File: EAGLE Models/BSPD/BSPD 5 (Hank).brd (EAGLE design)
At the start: 15.2 x 102.9 mm, 23 parts, among them IC1 LT1236S-5

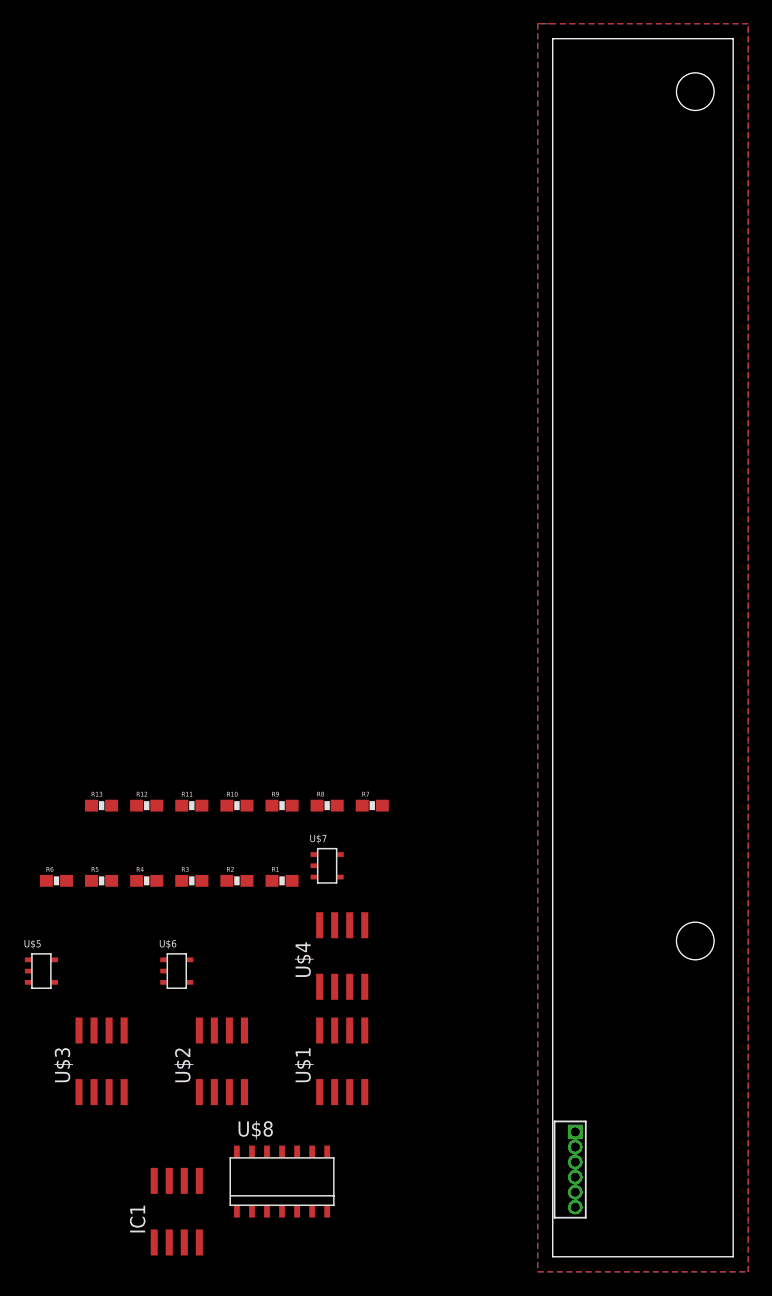
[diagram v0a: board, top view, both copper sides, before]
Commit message: BSPD board layout
Version 1, laying out v2 that should be theorectically more organized
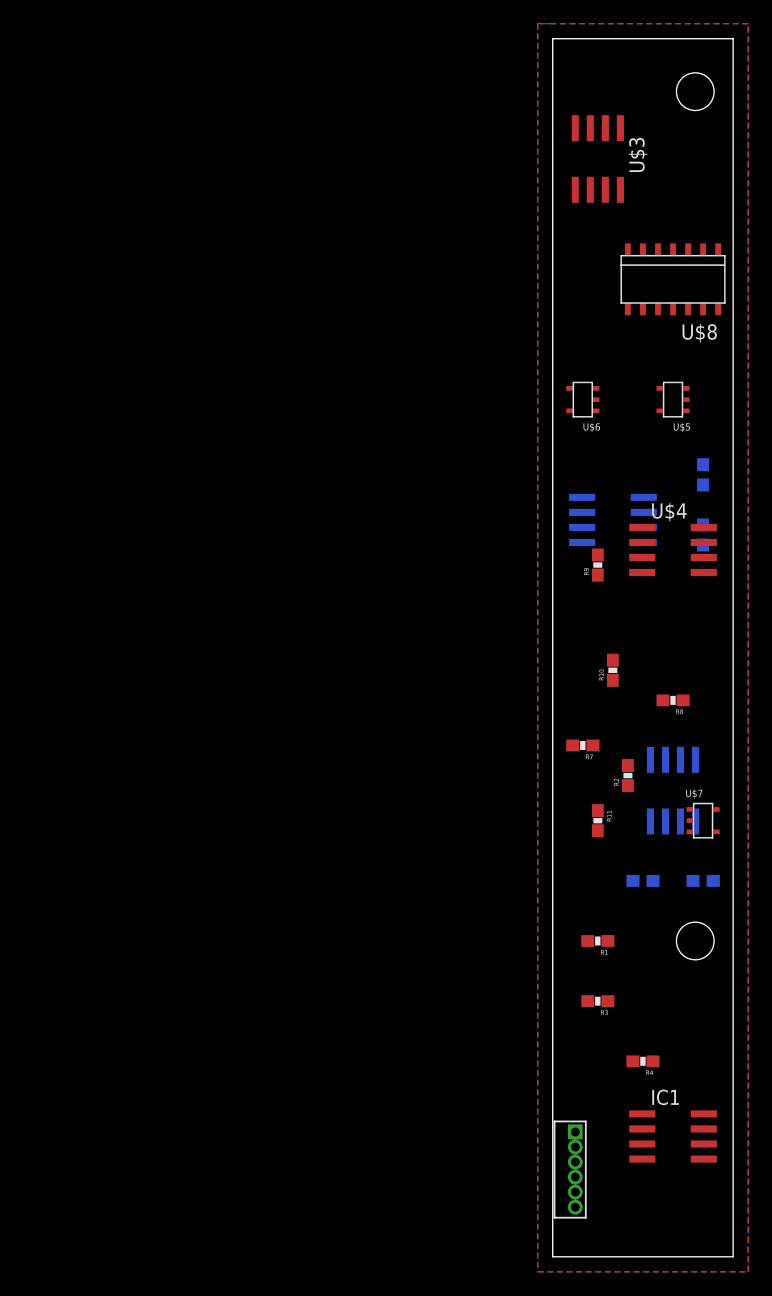
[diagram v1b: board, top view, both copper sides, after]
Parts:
- moved U$3 87.0 mm to (3.81, 92.7), turned to 180 degrees
- moved U$8 83.0 mm to (10.2, 82.5), turned to 180 degrees
- moved U$5 71.9 mm to (10.2, 72.4), turned to 180 degrees
- moved R6 64.5 mm to (12.7, 66.0), flipped to the bottom, turned to 270 degrees
- moved U$6 59.2 mm to (2.54, 72.4), turned to 180 degrees
- moved R5 58.6 mm to (12.7, 61.0), flipped to the bottom, turned to 270 degrees
- moved R13 51.2 mm to (12.7, 31.8), flipped to the bottom
- moved U$1 51.1 mm to (5.08, 62.2), flipped to the bottom, turned to 90 degrees
- moved R4 44.6 mm to (7.62, 16.5), turned to 180 degrees
- moved U$2 44.4 mm to (10.2, 39.4), flipped to the bottom, turned to 180 degrees
- moved U$4 44.2 mm to (10.2, 59.7), turned to 270 degrees
- moved IC1 42.4 mm to (10.2, 10.2), turned to 270 degrees
- moved R12 42.4 mm to (7.62, 31.8), flipped to the bottom, turned to 180 degrees
- moved R3 35.8 mm to (3.81, 21.6), turned to 180 degrees
- moved R11 34.3 mm to (3.81, 36.8), turned to 270 degrees
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
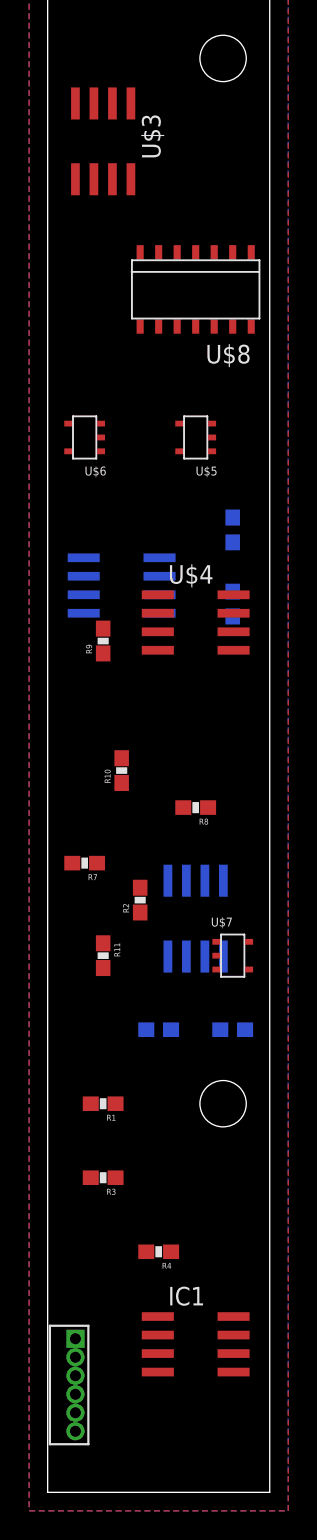
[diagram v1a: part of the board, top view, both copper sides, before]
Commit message: General layout of BSPD
Version 2, needs optimization
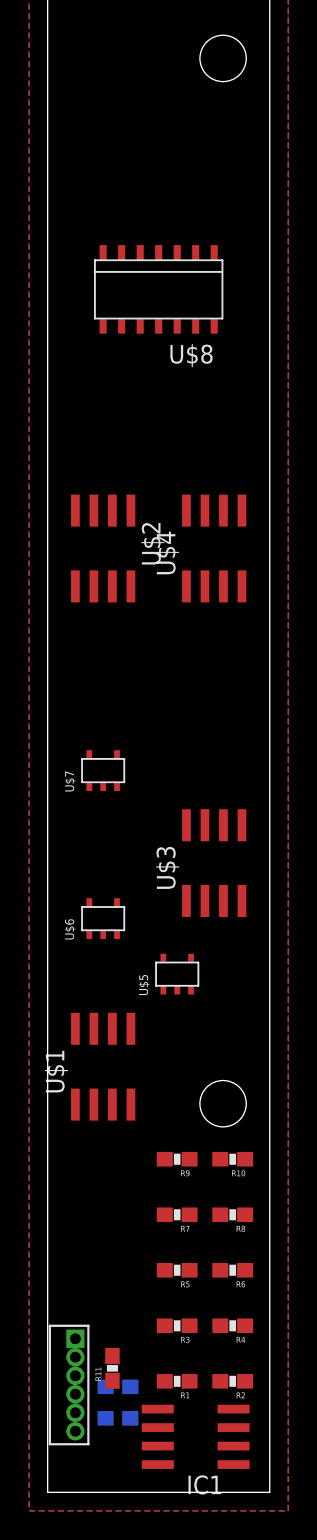
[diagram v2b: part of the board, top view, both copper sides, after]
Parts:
- moved R6 50.8 mm to (12.7, 15.2), flipped to the top, turned to 180 degrees
- moved U$3 50.1 mm to (11.4, 43.2), turned to 0 degrees
- moved R5 45.9 mm to (8.89, 15.2), flipped to the top, turned to 180 degrees
- moved U$5 36.9 mm to (8.89, 35.6), turned to 90 degrees
- moved R9 35.9 mm to (8.89, 22.9), turned to 180 degrees
- moved R2 33.6 mm to (12.7, 7.62), turned to 180 degrees
- moved U$6 33.0 mm to (3.81, 39.4), turned to 90 degrees
- moved U$1 33.0 mm to (3.81, 29.2), flipped to the top, turned to 0 degrees
- moved R11 28.3 mm to (4.45, 8.51), turned to 90 degrees
- moved R8 28.1 mm to (12.7, 19.1)
- moved R13 27.8 mm to (4.83, 5.08), turned to 180 degrees
- moved R10 27.7 mm to (12.7, 22.9), turned to 180 degrees
- moved U$2 26.2 mm to (3.81, 64.8), flipped to the top
- moved R7 25.0 mm to (8.89, 19.1)
- moved R12 24.7 mm to (4.83, 7.24)
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
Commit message: BSPD in process of optimization
:D
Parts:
- moved U$8 32.0 mm to (7.37, 50.5)
- moved U$2 22.7 mm to (5.84, 42.2)
- moved U$4 22.6 mm to (10.9, 42.2)
- moved U$7 14.8 mm to (4.57, 34.8)
- moved U$5 10.2 mm to (3.56, 26.9)
- moved U$1 9.67 mm to (4.32, 19.6)
- moved U$3 9.20 mm to (10.4, 34.0)
- moved U$6 8.16 mm to (4.57, 31.2)
- moved R2 8.13 mm to (6.35, 12.7), turned to 270 degrees
- moved R5 6.84 mm to (12.4, 9.40), turned to 270 degrees
- moved R9 6.62 mm to (12.4, 17.3), turned to 270 degrees
- moved R8 3.88 mm to (9.40, 21.1), turned to 270 degrees
- moved R4 3.54 mm to (9.40, 12.7), turned to 270 degrees
- moved R1 3.10 mm to (6.35, 9.40), turned to 270 degrees
- moved R6 2.55 mm to (12.4, 12.7), turned to 270 degrees
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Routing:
- net ALL_OK: track 0.00 -> 67.0 mm, vias 0 -> 1
- net N$1: track 0.00 -> 24.1 mm
- net 12V: track 0.00 -> 18.4 mm
- net 1.06V: track 0.00 -> 5.77 mm
- net CURRENT: track 0.00 -> 3.33 mm
- net BR: track 0.00 -> 2.33 mm
- net BF: track 0.00 -> 2.28 mm
- net .831V: track 0.00 -> 2.11 mm
- net 4.5V: track 0.00 -> 1.60 mm
- net 2.95V: track 0.00 -> 1.60 mm
- net .5V: track 0.00 -> 1.60 mm

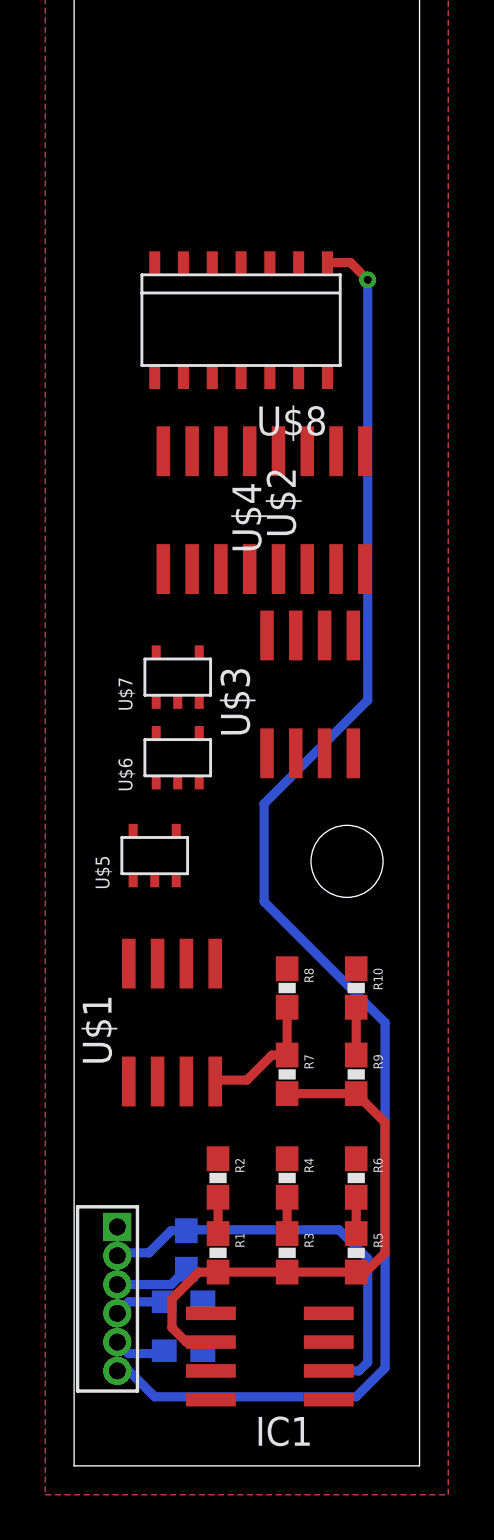
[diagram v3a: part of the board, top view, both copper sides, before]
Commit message: Routed BSPD
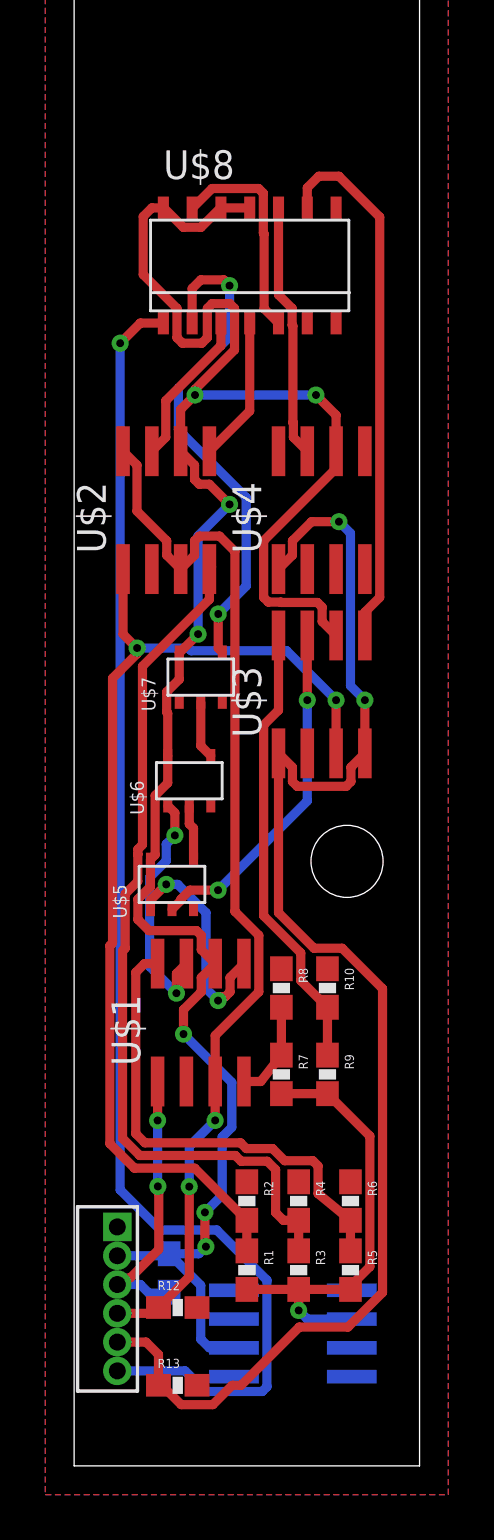
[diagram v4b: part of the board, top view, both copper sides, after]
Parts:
- moved U$8 2.44 mm to (7.75, 53.0), turned to 0 degrees
- moved U$2 1.78 mm to (4.06, 42.2), turned to 0 degrees
- moved R2 1.63 mm to (7.62, 11.7)
- moved R13 1.55 mm to (4.57, 3.56), flipped to the top, turned to 0 degrees
- moved R1 1.48 mm to (7.62, 8.64)
- moved U$5 1.48 mm to (4.32, 25.7)
- moved IC1 1.44 mm to (9.65, 5.84), flipped to the bottom
- moved U$1 1.27 mm to (5.59, 19.6)
- moved R11 1.27 mm to (4.19, 8.51)
- moved R10 1.27 mm to (11.2, 21.1)
- moved R9 1.27 mm to (11.2, 17.3)
- moved U$6 1.14 mm to (5.08, 30.2)
- moved R4 1.14 mm to (9.91, 11.7)
- moved R6 1.05 mm to (12.2, 11.7)
- moved U$7 1.02 mm to (5.59, 34.8)
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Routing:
- net 12V: track 18.4 -> 95.9 mm, vias 0 -> 7
- net BR: track 2.33 -> 62.5 mm, vias 0 -> 2
- net BF: track 2.28 -> 47.9 mm, vias 0 -> 2
- net 4.5V: track 1.60 -> 47.0 mm, vias 0 -> 2
- net .5V: track 1.60 -> 38.6 mm
- net N$11: track 0.00 -> 23.8 mm
- net N$7: track 0.00 -> 22.4 mm, vias 0 -> 2
- net 2.95V: track 1.60 -> 21.3 mm
- net .831V: track 2.11 -> 20.0 mm
- net N$3: track 0.00 -> 15.3 mm, vias 0 -> 2
- net N$12: track 0.00 -> 11.3 mm
- net N$5: track 0.00 -> 10.8 mm, vias 0 -> 2
- net N$2: track 0.00 -> 9.95 mm, vias 0 -> 2
- net N$10: track 0.00 -> 9.59 mm
- net CURRENT: track 3.33 -> 12.4 mm, vias 0 -> 2
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
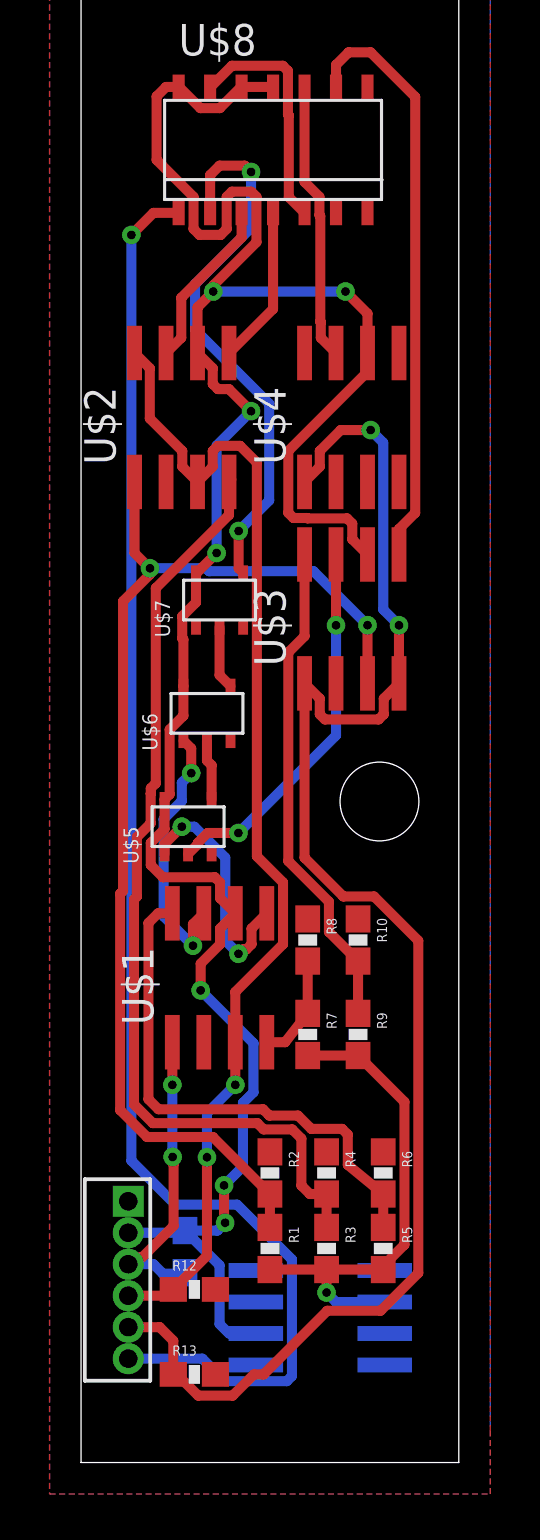
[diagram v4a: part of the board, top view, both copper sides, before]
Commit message: BSPD board fully wired
Grounding issues awaiting resolution
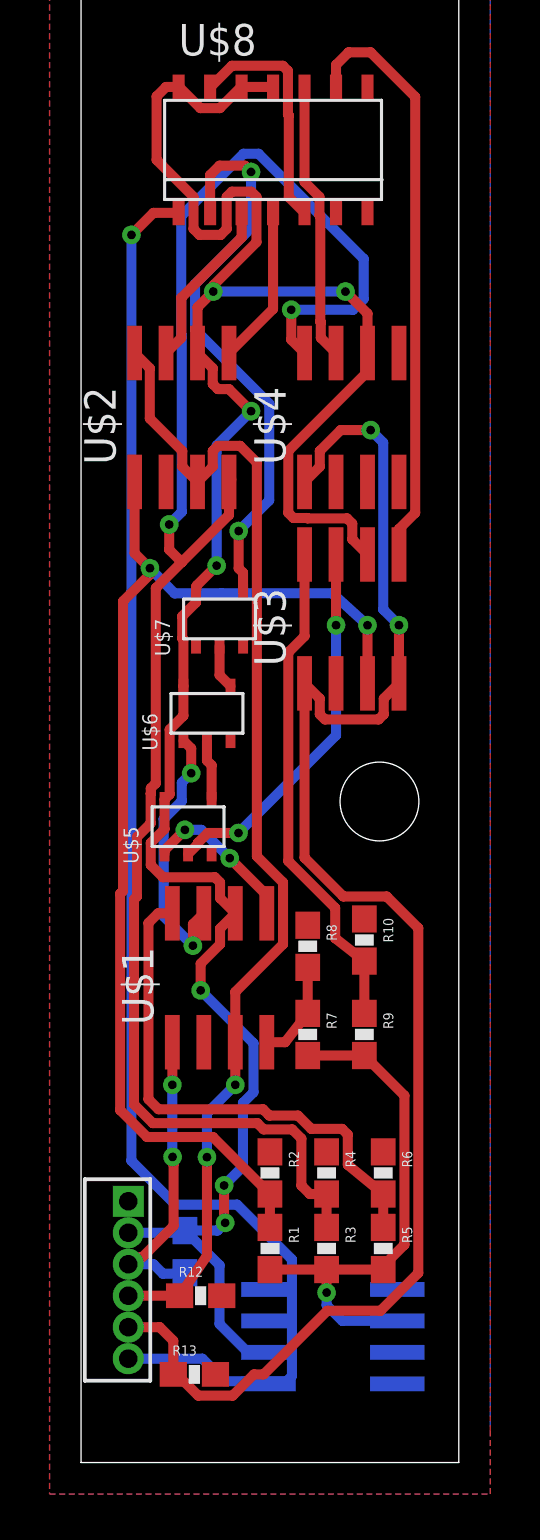
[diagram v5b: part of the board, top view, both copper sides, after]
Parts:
- moved IC1 0.92 mm to (10.2, 5.08)
- moved U$7 0.76 mm to (5.59, 34.0)
- moved R12 0.36 mm to (4.83, 6.73)
- moved R8 0.25 mm to (9.14, 20.8)
- moved R10 0.25 mm to (11.4, 21.1)
- moved R9 0.25 mm to (11.4, 17.3)
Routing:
- net .5V: track 38.6 -> 69.8 mm, vias 0 -> 2
- net N$2: track 9.95 -> 6.44 mm
- net N$1: track 19.8 -> 21.1 mm
- net 12V: track 95.9 -> 96.7 mm
- net N$7: track 22.4 -> 23.1 mm
- net N$6: track 2.56 -> 1.79 mm
